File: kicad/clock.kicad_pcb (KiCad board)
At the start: 2 copper layers, 100 x 100 mm, 48 parts, among them SW2 SW_DIP_x08, SW3 SW_Push, SW4 SW_Push, U1 74HC04, U11 7SEGMENT_CC, U12 4543, U13 7SEGMENT_CC, U14 4543, U17 7SEGMENT_CC, U18 74LS390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

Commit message: All but beep routing done
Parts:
- removed R14: 22k, Resistors_THT:R_Axial_DIN0207_L6.3mm_D2.5mm_P10.16mm_Horizontal
- added SW1: SW_Push, Buttons_Switches_THT:SW_TH_Tactile_Omron_B3F-10xx, F.Cu at (172.7, 96.0)
- added TP1: 0.5 Hz, clock:TestPoint, F.Cu at (137.9, 120.4)
- added TP1: 0.5 Hz, clock:TestPoint, F.Cu at (143.1, 74.3)
- added TP1: 0.5 Hz, clock:TestPoint, F.Cu at (145.5, 74.3)
- added TP1: 0.5 Hz, clock:TestPoint, F.Cu at (137.8, 79.0)
- added TP1: 0.5 Hz, clock:TestPoint, F.Cu at (100.3, 63.1)
- added TP1: 0.5 Hz, clock:TestPoint, F.Cu at (105.4, 63.1)
- added TP1: 0.5 Hz, clock:TestPoint, F.Cu at (110.5, 63.1)
- added TP1: 0.5 Hz, clock:TestPoint, F.Cu at (118.1, 52.2)
- added TP1: 0.5 Hz, clock:TestPoint, F.Cu at (109.2, 52.2)
- added TP1: 0.5 Hz, clock:TestPoint, F.Cu at (100.3, 52.2)
- added TP1: 0.5 Hz, clock:TestPoint, F.Cu at (118.1, 49.4)
- added TP1: 0.5 Hz, clock:TestPoint, F.Cu at (157.6, 122.9)
- added TP1: 0.5 Hz, clock:TestPoint, F.Cu at (109.2, 49.4)
- added TP1: 0.5 Hz, clock:TestPoint, F.Cu at (100.3, 49.4)
- added TP1: 0.5 Hz, clock:TestPoint, F.Cu at (163.2, 119.8)
- added TP1: 0.5 Hz, clock:TestPoint, F.Cu at (133.3, 114.6)
- added TP1: 0.5 Hz, clock:TestPoint, F.Cu at (133.3, 112.0)
- added TP1: 0.5 Hz, clock:TestPoint, F.Cu at (137.9, 122.9)
- added TP1: 0.5 Hz, clock:TestPoint, F.Cu at (110.5, 60.1)
- added TP1: 0.5 Hz, clock:TestPoint, F.Cu at (157.9, 101.9)
- added TP1: 0.5 Hz, clock:TestPoint, F.Cu at (157.9, 112.0)
- added TP1: 0.5 Hz, clock:TestPoint, F.Cu at (157.9, 104.4)
- added U10: Discrete_NAND, Housings_DIP:DIP-6_W7.62mm, F.Cu at (97.8, 54.6)
- added U15: Discrete_NAND, Housings_DIP:DIP-6_W7.62mm, F.Cu at (106.7, 54.6)
- added U16: Discrete_NAND, Housings_DIP:DIP-6_W7.62mm, F.Cu at (115.6, 54.6)
- SW3: moved to B.Cu
- moved C4 199.0 mm to (78.5, 141.6)
- moved R17 190.3 mm to (73.2, 148.2)
- moved R15 187.9 mm to (74.5, 154.1)
- moved U21 187.5 mm to (76.9, 125.0)
- moved U1 165.8 mm to (97.8, 65.4), turned to 90 degrees
- moved U18 146.6 mm to (97.8, 76.5), turned to 90 degrees
- moved C5 119.3 mm to (120.7, 64.8), turned to 90 degrees
- moved R16 113.1 mm to (120.7, 82.3), turned to 270 degrees
- moved R18 108.4 mm to (120.7, 80.0), turned to 90 degrees
- moved D1 105.8 mm to (110.2, 91.2), turned to 180 degrees
- moved R13 99.5 mm to (101.3, 94.7)
- moved C3 92.0 mm to (120.7, 95.8), turned to 270 degrees
- moved SW4 58.4 mm to (108.5, 106.7), turned to 90 degrees
- moved SW3 49.7 mm to (104.4, 106.7), turned to 90 degrees
- moved U19 27.4 mm to (97.8, 87.6), turned to 90 degrees
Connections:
- U1 pad 1: (no net) -> Net-(U1-Pad1)
- U1 pad 3: (no net) -> Net-(U1-Pad3)
- U1 pad 5: (no net) -> Net-(U1-Pad5)
- U3 pad 7: (no net) -> Net-(SW1-Pad1)
- U8 pad 11: (no net) -> Net-(U15-Pad5)
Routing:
- net GND: track 339.0 -> 569.5 mm
- net VCC: track 248.4 -> 432.6 mm, vias 0 -> 1
- net PWM: track 32.9 -> 97.5 mm, vias 0 -> 2
- net Net-(C3-Pad1): track 0.00 -> 45.3 mm
- net 1min: track 16.2 -> 54.7 mm
- net HH1: track 60.5 -> 96.6 mm
- net Net-(D1-Pad2): track 0.00 -> 35.1 mm
- net 1Hz: track 8.62 -> 36.7 mm
- net Net-(U1-Pad11): track 0.00 -> 27.4 mm
- net Net-(U1-Pad3): track 0.00 -> 26.4 mm
- net ALM: track 0.00 -> 24.1 mm
- net Net-(SW1-Pad1): track 0.00 -> 16.7 mm
- net Net-(U1-Pad2): track 0.00 -> 16.6 mm
- net Net-(C5-Pad1): track 0.00 -> 16.4 mm
- net OFF: track 0.00 -> 16.0 mm
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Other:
- board text added: "Off"
- board text added: "Set"
- board text added: "Sleep"
- board text added: "a"
- board text added: "b"
- board text added: "c"
- board text added: "d"
- board text added: "e"
- board text added: "f"
- board text added: "g"
- board text added: "h"
- board text added: "i"
- board text added: "j"
- board text added: "k"

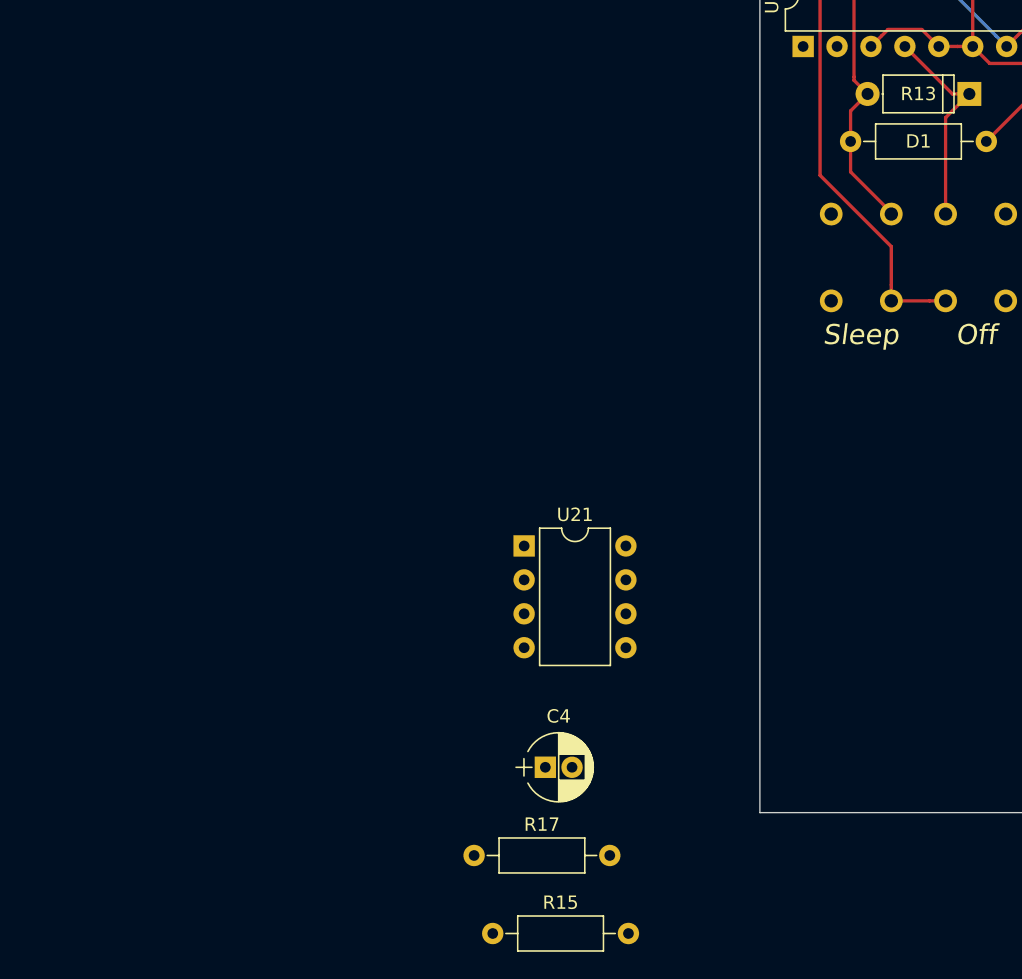
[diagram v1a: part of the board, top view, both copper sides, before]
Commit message: New beeping circuit
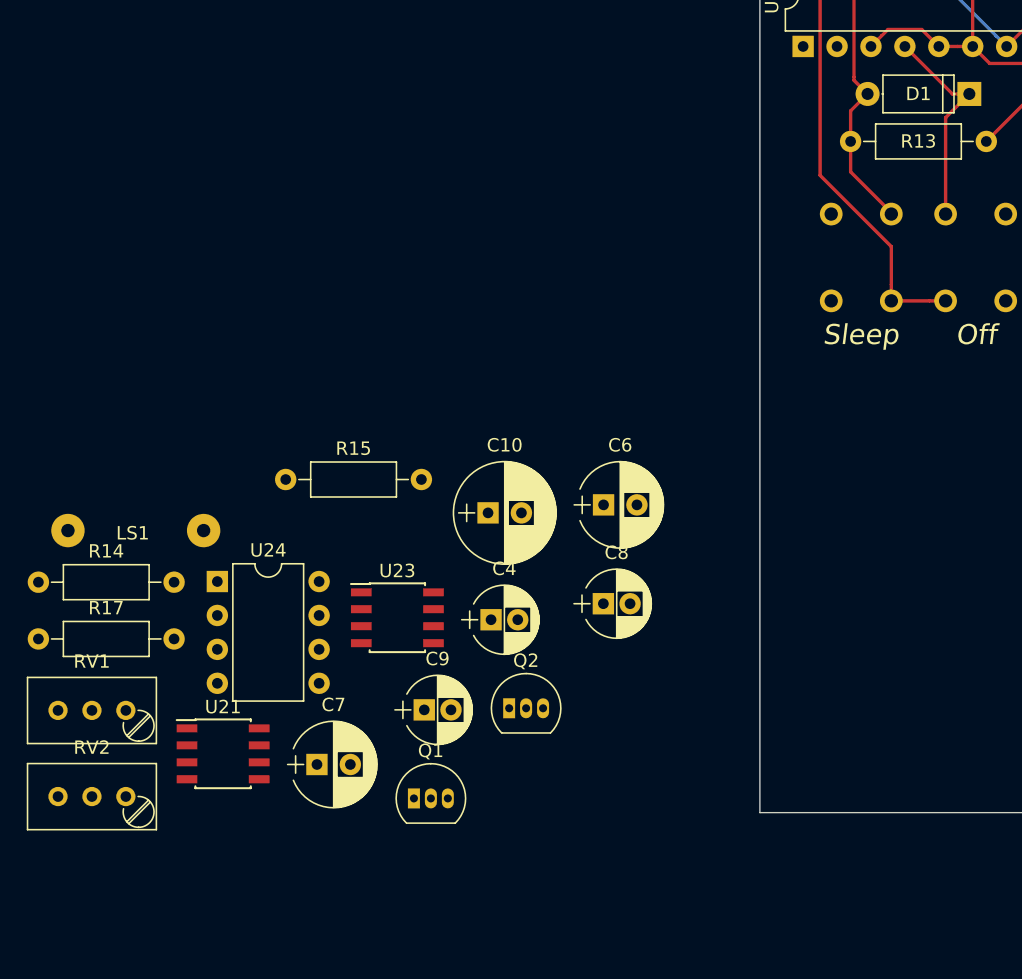
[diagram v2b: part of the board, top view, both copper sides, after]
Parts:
- added C10: 100u, Capacitors_THT:CP_Radial_D7.5mm_P2.50mm, F.Cu at (74.2, 122.6)
- added C6: 10u, Capacitors_THT:CP_Radial_D6.3mm_P2.50mm, F.Cu at (82.8, 122.0)
- added C7: 10u, Capacitors_THT:CP_Radial_D6.3mm_P2.50mm, F.Cu at (61.4, 141.4)
- added C8: 0u1, Capacitors_THT:CP_Radial_D5.0mm_P2.00mm, F.Cu at (82.8, 129.4)
- added C9: 0u1, Capacitors_THT:CP_Radial_D5.0mm_P2.00mm, F.Cu at (69.4, 137.3)
- added LS1: Beep, Wire_Connections_Bridges:WireConnection_1.00mmDrill, F.Cu at (42.7, 123.9)
- added Q1: PN2222A, TO_SOT_Packages_THT:TO-92_Inline_Narrow_Oval, F.Cu at (68.6, 143.9)
- added Q2: 2N3906, TO_SOT_Packages_THT:TO-92_Inline_Narrow_Oval, F.Cu at (75.8, 137.2)
- added R14: 22k, Resistors_THT:R_Axial_DIN0207_L6.3mm_D2.5mm_P10.16mm_Horizontal, F.Cu at (40.5, 127.7)
- added RV1: 50k, Potentiometers:Potentiometer_Trimmer_Bourns_3296W, F.Cu at (47.1, 137.3)
- added RV2: 10k, Potentiometers:Potentiometer_Trimmer_Bourns_3296W, F.Cu at (47.1, 143.8)
- added U23: TLC555CD, Housings_SOIC:SOIC-8_3.9x4.9mm_Pitch1.27mm, F.Cu at (67.4, 130.4)
- added U24: LM358, Housings_DIP:DIP-8_W7.62mm, F.Cu at (53.9, 127.7)
- C4: value 1u -> 0u1
- R15: value 2k2 -> 1k
- R17: value 2k2 -> 100k
- U21: value NE555 -> TLC555CD; footprint Housings_DIP:DIP-8_W7.62mm -> Housings_SOIC:SOIC-8_3.9x4.9mm_Pitch1.27mm
- moved R15 37.4 mm to (59.0, 120.1)
- moved R17 36.4 mm to (40.5, 132.0)
- moved U21 27.4 mm to (54.4, 140.6)
- moved C4 11.8 mm to (74.4, 130.6)
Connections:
- C4 pad 1: Net-(C4-Pad1) -> VCC
- R15 pad 1: VCC -> Net-(C6-Pad1)
- R17 pad 1: Net-(C4-Pad1) -> Net-(R15-Pad2)
- R17 pad 2: Net-(R15-Pad2) -> Net-(C7-Pad1)
- TP1 pad 1: Net-(U20-Pad19) -> 0.5Hz (x2)
- TP1 pad 1: 1hr -> 0.5Hz (x2)
- TP1 pad 1: MH1 -> 0.5Hz (x2)
- TP1 pad 1: HL1 -> 0.5Hz (x2)
- TP1 pad 1: Net-(U1-Pad2) -> 0.5Hz (x2)
- TP1 pad 1: Net-(U1-Pad4) -> 0.5Hz (x2)
- TP1 pad 1: Net-(U1-Pad6) -> 0.5Hz (x2)
- TP1 pad 1: HH1 -> 0.5Hz
- TP1 pad 1: 1min -> 0.5Hz (x2)
- TP1 pad 1: Net-(U15-Pad5) -> 0.5Hz (x2)
- TP1 pad 1: 1Hz -> 0.5Hz
- TP1 pad 1: Net-(U1-Pad9) -> 0.5Hz (x2)
- U19 pad 1: BEEP -> (no net)
- U19 pad 2: (no net) -> ~BEEP
- U21 pad 2: Net-(R15-Pad2) -> Net-(C7-Pad1)
- U21 pad 3: (no net) -> Net-(R15-Pad2)
- U21 pad 4: 1Hz -> ~BEEP
- U21 pad 6: Net-(R15-Pad2) -> Net-(C7-Pad1)
- U21 pad 7: Net-(C4-Pad1) -> (no net)
- U21 pad 8: BEEP -> VCC

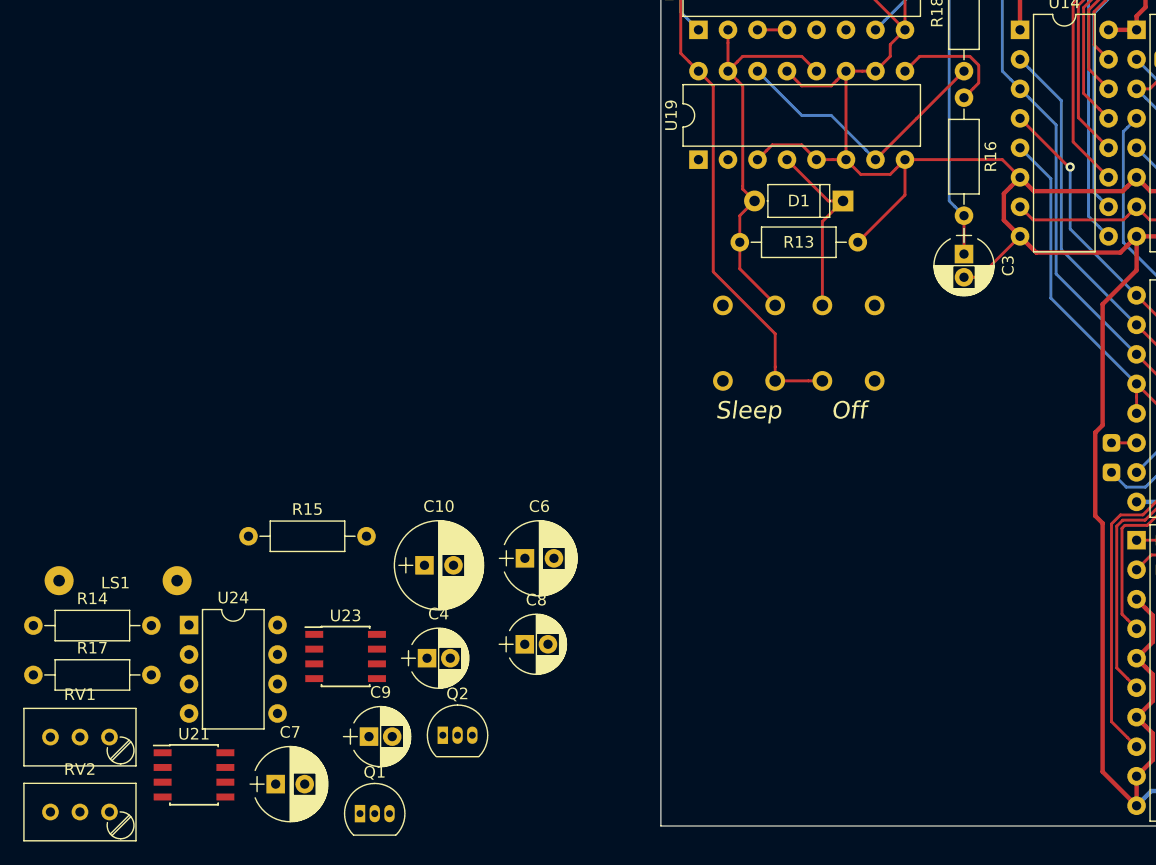
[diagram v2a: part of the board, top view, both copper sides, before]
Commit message: Beep circuit mostly routed
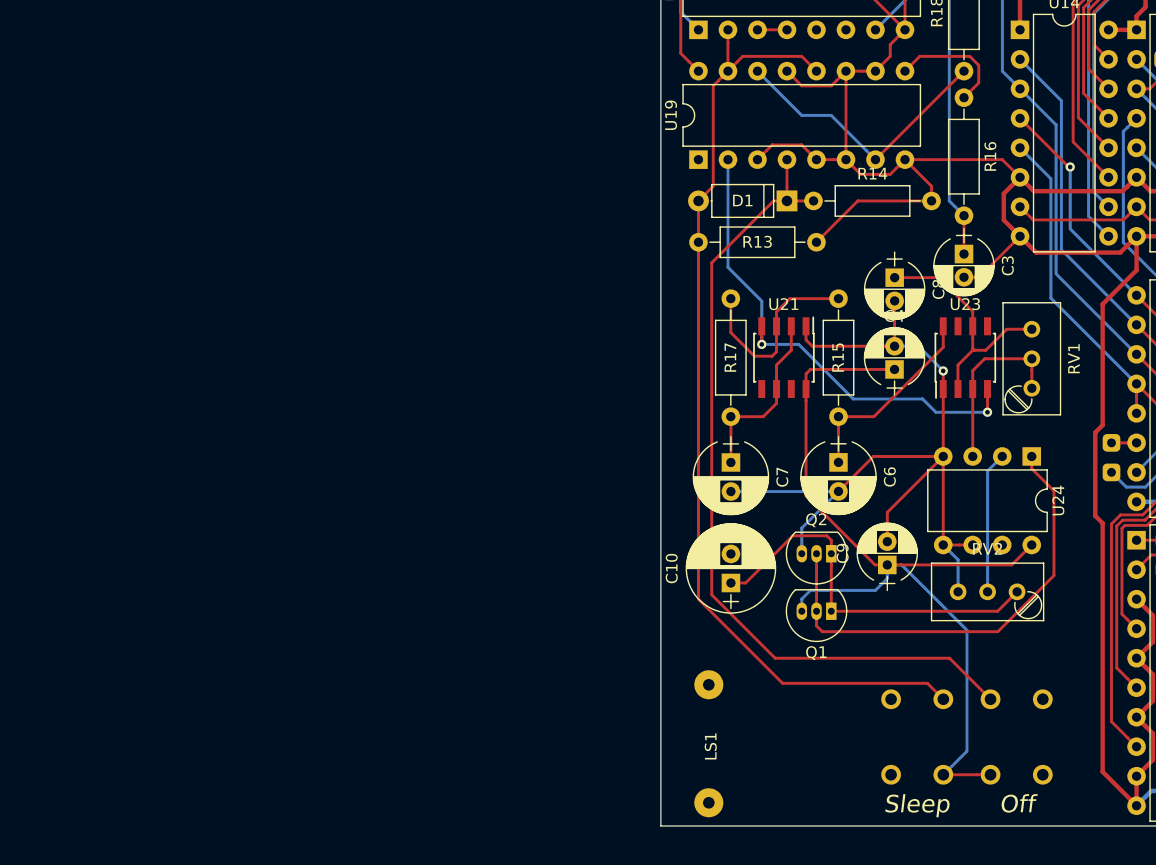
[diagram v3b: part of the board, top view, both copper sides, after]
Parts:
- moved RV1 84.9 mm to (126.5, 107.3), turned to 270 degrees
- moved RV2 80.4 mm to (125.2, 124.8)
- moved R14 76.5 mm to (107.7, 91.2)
- moved U24 74.0 mm to (126.5, 113.2), turned to 270 degrees
- moved R17 68.2 mm to (100.6, 99.6), turned to 270 degrees
- moved U21 62.2 mm to (105.1, 104.7), turned to 270 degrees
- moved U23 59.2 mm to (120.8, 104.7), turned to 90 degrees
- moved LS1 59.1 mm to (98.7, 143.0), turned to 90 degrees
- moved R15 51.8 mm to (109.8, 109.8), turned to 90 degrees
- moved C7 48.0 mm to (100.6, 113.7), turned to 270 degrees
- moved C4 47.3 mm to (114.7, 105.7), turned to 90 degrees
- moved C9 47.0 mm to (114.0, 122.5), turned to 90 degrees
- moved C8 44.8 mm to (114.7, 97.8), turned to 270 degrees
- moved Q1 44.2 mm to (109.2, 126.5), turned to 180 degrees
- moved Q2 36.9 mm to (109.2, 121.6), turned to 180 degrees
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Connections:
- U24 pad 5: (no net) -> GND
- U24 pad 6: (no net) -> GND
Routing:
- net GND: track 569.5 -> 652.2 mm, vias 0 -> 1
- net OFF: track 16.0 -> 70.8 mm
- net Net-(D1-Pad2): track 35.1 -> 83.5 mm
- net VCC: track 432.6 -> 476.9 mm
- net ~BEEP: track 0.00 -> 42.5 mm, vias 0 -> 2
- net Net-(Q1-Pad2): track 0.00 -> 39.9 mm
- net Net-(C10-Pad1): track 0.00 -> 33.3 mm
- net Net-(C8-Pad1): track 0.00 -> 21.2 mm
- net Net-(C6-Pad1): track 0.00 -> 17.2 mm
- net Net-(R15-Pad2): track 0.00 -> 17.1 mm
- net Net-(C7-Pad1): track 0.00 -> 15.5 mm
- net Net-(RV1-Pad1): track 0.00 -> 15.4 mm
- net Net-(RV2-Pad2): track 0.00 -> 12.2 mm

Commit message: Routing done: need board edges
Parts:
- added J1: Conn_01x02_Female, Wire_Pads:SolderWirePad_2x_1mmDrill, F.Cu at (97.3, 139.6)
- moved LS1 10.0 mm to (97.3, 133.1), turned to 45 degrees
- moved SW3 8.89 mm to (110.0, 140.6)
- moved SW4 3.18 mm to (119.8, 140.6)
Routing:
- net VCC: track 476.9 -> 497.2 mm
- net GND: track 652.2 -> 672.2 mm
- net Net-(C10-Pad2): track 0.00 -> 12.9 mm
- net Net-(D1-Pad2): track 83.5 -> 76.7 mm
- net OFF: track 70.8 -> 69.5 mm
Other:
- copper layers 2 -> 4
